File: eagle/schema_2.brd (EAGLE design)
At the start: 49.5 x 69.8 mm, 39 parts, among them IC2 BTS428L2

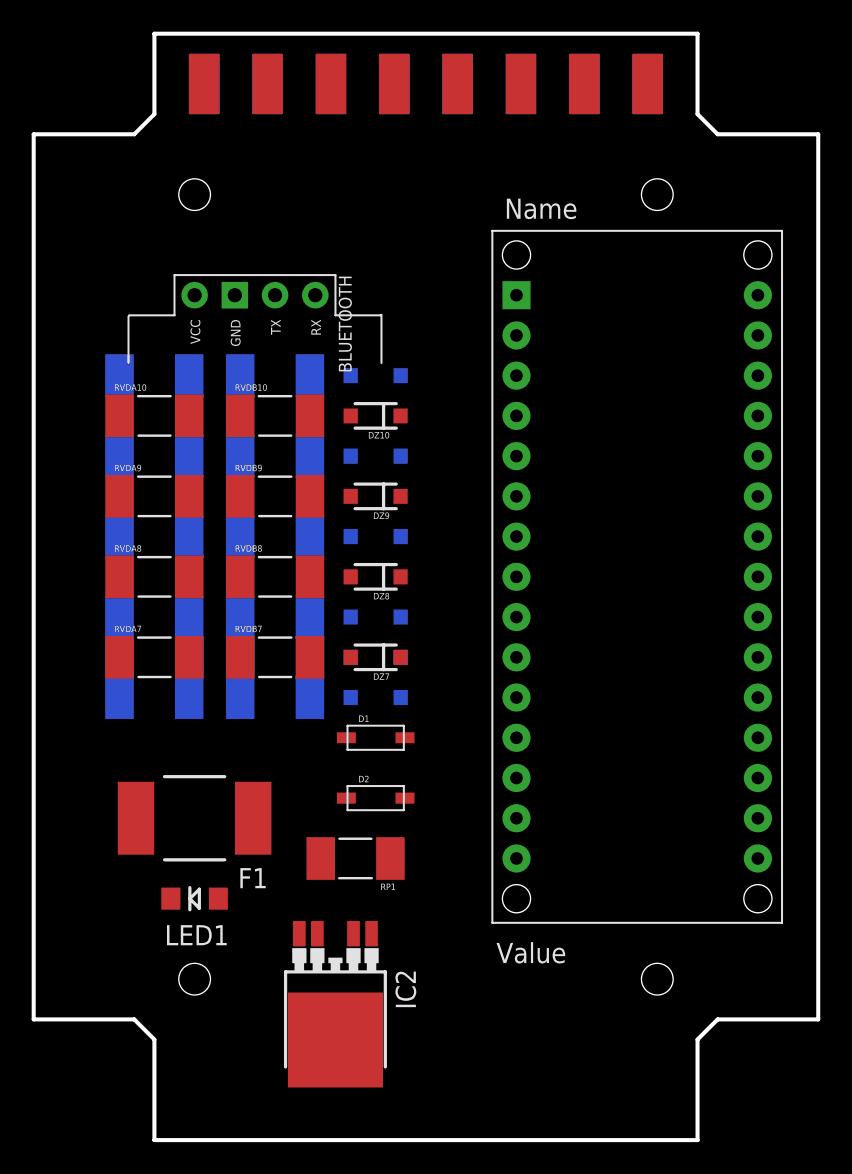
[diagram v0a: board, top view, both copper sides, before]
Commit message: Layout change
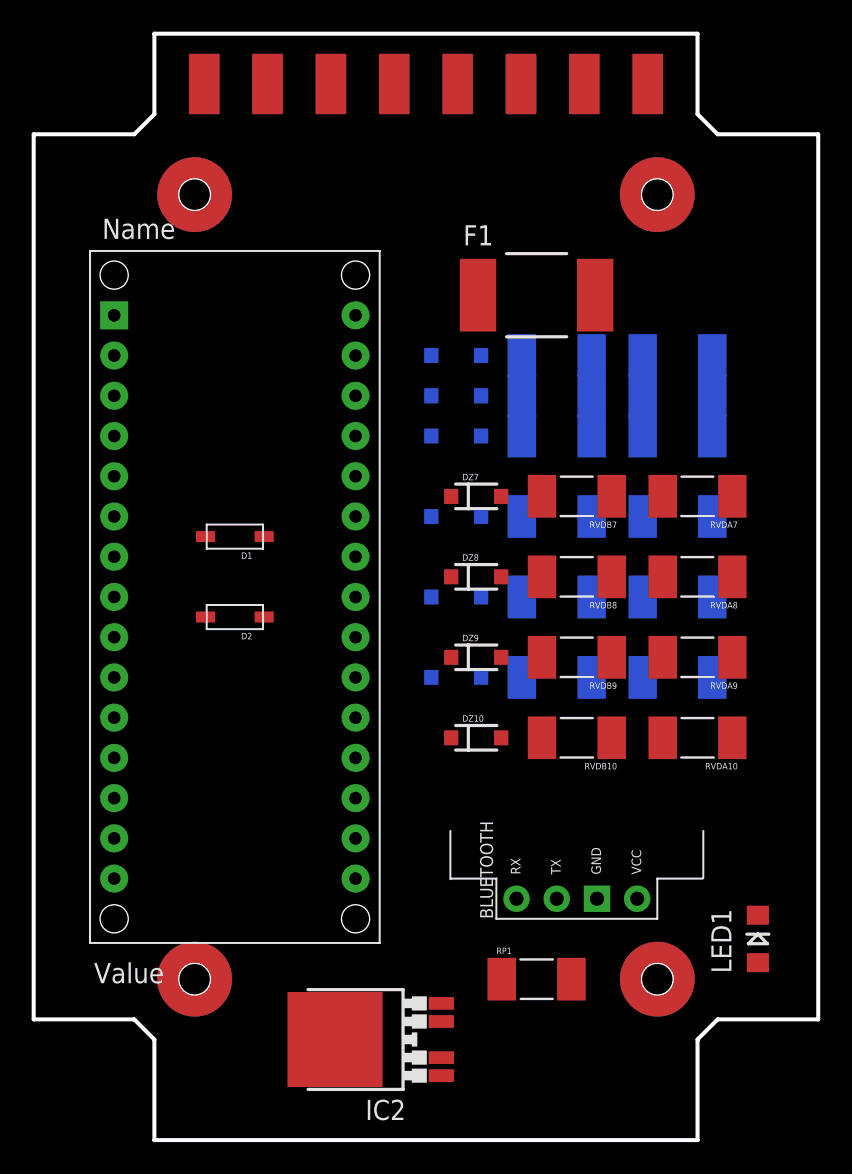
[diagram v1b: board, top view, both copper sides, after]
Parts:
- moved RVDA10 39.9 mm to (41.9, 25.4), turned to 180 degrees
- moved F1 39.5 mm to (31.8, 53.3), turned to 0 degrees
- moved RVDA2 39.5 mm to (40.6, 49.5), turned to 0 degrees
- moved RVDA6 38.1 mm to (40.6, 29.2), turned to 0 degrees
- moved RVDA1 36.9 mm to (40.6, 47.0), turned to 0 degrees
- moved BLUETOOTH 36.6 mm to (34.3, 19.1), turned to 90 degrees
- moved RVDA7 35.8 mm to (41.9, 40.6), turned to 180 degrees
- moved RVDA9 35.8 mm to (41.9, 30.5), turned to 180 degrees
- moved LED1 35.7 mm to (45.7, 12.7), turned to 90 degrees
- moved RVDA3 34.9 mm to (40.6, 44.5), turned to 0 degrees
- moved RVDA8 34.3 mm to (41.9, 35.6), turned to 180 degrees
- moved RVDA5 34.2 mm to (40.6, 34.3), turned to 0 degrees
- moved RVDA4 33.0 mm to (40.6, 39.4), turned to 0 degrees
- moved RVDB2 28.0 mm to (33.0, 49.5), turned to 0 degrees
- moved RVDB10 27.9 mm to (34.3, 25.4), turned to 180 degrees
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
